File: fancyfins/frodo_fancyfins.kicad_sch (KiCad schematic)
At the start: 102 parts, among them J3 TC2050, U1 AZ1117-5.0, U10 L78L05_SOT89, U11 W25Q128JVP, U12 L78L05_SOT89, U13 L78L05_SOT89, U14 L78L05_SOT89, U15 L78L05_SOT89, U16 L78L05_SOT89, U2 AZ1117-3.3, U3 STM32F103RCTx, U4 MCP2562-E-SN, U5 TPD4E1U06, U6 L78L05_SOT89, U7 L78L05_SOT89, U8 L78L05_SOT89, U9 L78L05_SOT89, Y1 8MHz 12pF

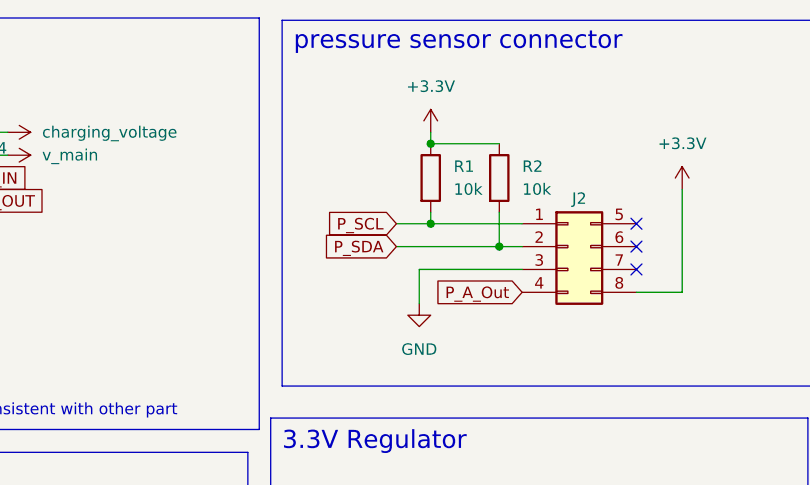
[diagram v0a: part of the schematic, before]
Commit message: finalized fancyfin routing (for now)
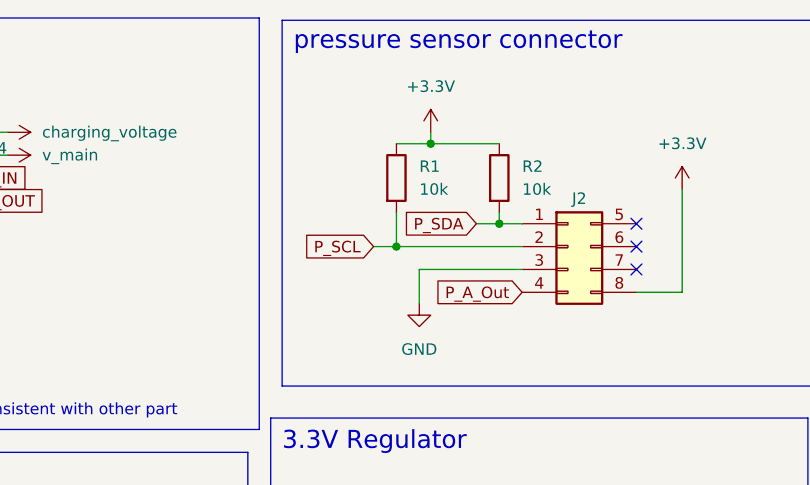
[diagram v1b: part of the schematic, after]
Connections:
- net P_SCL: now also J2.2 (Pin_2); no longer J2.1 (Pin_1)
- net P_SDA: now also J2.1 (Pin_1); no longer J2.2 (Pin_2)
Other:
- moved on the sheet: R1
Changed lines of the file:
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@@
 	)
 	(junction
+		(at 115.57 36.83)
+		(diameter 0)
+		(color 0 0 0 0)
+	)
+	(junction
 		(at 121.92 83.82)
 		(diameter 0)
@@
 	)
 	(junction
-		(at 107.95 36.83)
-		(diameter 0)
-		(color 0 0 0 0)
-	)
-	(junction
 		(at 46.99 214.63)
 		(diameter 0)
@@
 	)
 	(junction
-		(at 115.57 39.37)
-		(diameter 0)
-		(color 0 0 0 0)
-	)
-	(junction
 		(at 327.66 148.59)
 		(diameter 0)
@@
 	)
 	(junction
+		(at 104.14 39.37)
+		(diameter 0)
+		(color 0 0 0 0)
+	)
+	(junction
 		(at 109.22 231.14)
 		(diameter 0)
@@
 	(wire
 		(pts
-			(xy 107.95 35.56) (xy 107.95 36.83)
+			(xy 104.14 35.56) (xy 104.14 39.37)
 		)
 		(stroke
@@
 	(wire
 		(pts
-			(xy 104.14 39.37) (xy 115.57 39.37)
+			(xy 113.03 36.83) (xy 115.57 36.83)
 		)
 		(stroke
@@
 	(wire
 		(pts
-			(xy 115.57 35.56) (xy 115.57 39.37)
+			(xy 115.57 35.56) (xy 115.57 36.83)
 		)
 		(stroke
@@
 	(wire
 		(pts
+			(xy 115.57 36.83) (xy 118.11 36.83)
+		)
+		(stroke
+			(width 0)
+			(type default)
+		)
+	)
+	(wire
+		(pts
 			(xy 195.58 241.3) (xy 195.58 257.81)
 		)
@@
 	(wire
 		(pts
-			(xy 72.39 223.52) (xy 72.39 224.79)
+			(xy 104.14 27.94) (xy 107.95 27.94)
 		)
 		(stroke
@@
 	(wire
 		(pts
-			(xy 358.14 220.98) (xy 358.14 218.44)
+			(xy 72.39 223.52) (xy 72.39 224.79)
 		)
 		(stroke
@@
 	(wire
 		(pts
-			(xy 226.06 231.14) (xy 251.46 231.14)
+			(xy 358.14 220.98) (xy 358.14 218.44)
 		)
 		(stroke
@@
 	(wire
 		(pts
-			(xy 364.49 148.59) (xy 364.49 149.86)
+			(xy 226.06 231.14) (xy 251.46 231.14)
 		)
 		(stroke
@@
 	(wire
 		(pts
-			(xy 190.5 161.29) (xy 205.74 161.29)
+			(xy 364.49 148.59) (xy 364.49 149.86)
 		)
 		(stroke
@@
 	(wire
 		(pts
-			(xy 351.79 121.92) (xy 354.33 121.92)
+			(xy 190.5 161.29) (xy 205.74 161.29)
 		)
 		(stroke
@@
 	(wire
 		(pts
-			(xy 369.57 69.85) (xy 379.73 69.85)
+			(xy 351.79 121.92) (xy 354.33 121.92)
 		)
 		(stroke
@@
 	(wire
 		(pts
-			(xy 115.57 39.37) (xy 118.11 39.37)
+			(xy 369.57 69.85) (xy 379.73 69.85)
 		)
 		(stroke
@@
 	(wire
 		(pts
-			(xy 104.14 36.83) (xy 107.95 36.83)
+			(xy 101.6 39.37) (xy 104.14 39.37)
 		)
 		(stroke
@@
 	(wire
 		(pts
-			(xy 107.95 36.83) (xy 118.11 36.83)
-		)
-		(stroke
-			(width 0)
-			(type default)
-		)
-	)
-	(wire
-		(pts
 			(xy 142.24 224.79) (xy 142.24 223.52)
 		)
@@
 	(wire
 		(pts
+			(xy 104.14 39.37) (xy 118.11 39.37)
+		)
+		(stroke
+			(width 0)
+			(type default)
+		)
+	)
+	(wire
+		(pts
 			(xy 33.02 29.21) (xy 34.29 29.21)
 		)
@@
 	(global_label "P_SCL"
 		(shape input)
-		(at 104.14 36.83 180)
+		(at 101.6 39.37 180)
 		(fields_autoplaced yes)
 		(effects
@@
 		)
 		(property "Intersheetrefs" "${INTERSHEET_REFS}"
-			(at 95.4096 36.83 0)
+			(at 92.8696 39.37 0)
 			(effects
 				(font
@@
 	(global_label "P_SDA"
 		(shape input)
-		(at 104.14 39.37 180)
+		(at 113.03 36.83 180)
 		(fields_autoplaced yes)
 		(effects
@@
 		)
 		(property "Intersheetrefs" "${INTERSHEET_REFS}"
-			(at 95.3491 39.37 0)
+			(at 104.2391 36.83 0)
 			(effects
 				(font
@@
 	(symbol
 		(lib_id "Device:R")
-		(at 107.95 31.75 0)
+		(at 104.14 31.75 0)
 		(unit 1)
 		(exclude_from_sim no)
@@
 		(fields_autoplaced yes)
 		(property "Reference" "R1"
-			(at 110.49 30.4799 0)
+			(at 106.68 30.4799 0)
 			(effects
 				(font
@@
 		)
 		(property "Value" "10k"
-			(at 110.49 33.0199 0)
+			(at 106.68 33.0199 0)
 			(effects
 				(font
@@
 		)
 		(property "Footprint" "Resistor_SMD:R_0402_1005Metric"
-			(at 106.172 31.75 90)
+			(at 102.362 31.75 90)
 			(effects
 				(font
@@
 		)
 		(property "Datasheet" "~"
-			(at 107.95 31.75 0)
+			(at 104.14 31.75 0)
 			(effects
 				(font
@@
 		)
 		(property "Description" "Resistor"
-			(at 107.95 31.75 0)
+			(at 104.14 31.75 0)
 			(effects
 				(font

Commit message: finished routing for fin board
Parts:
- removed C17: 1u, Capacitor_SMD:C_0603_1608Metric_Pad1.08x0.95mm_HandSolder, symbol Device:C
- added C1: 330n, Capacitor_SMD:C_0402_1005Metric, symbol Device:C_Small
- added C2, C6, C7: 100n, Capacitor_SMD:C_0402_1005Metric, symbol Device:C_Small
- added C21: 1u, Capacitor_SMD:C_0402_1005Metric, symbol Device:C
- added JP1: SolderJumper_3_Open, Jumper:SolderJumper-3_P1.3mm_Open_RoundedPad1.0x1.5mm, symbol Jumper:SolderJumper_3_Open
- added R3: 10k, Resistor_SMD:R_0402_1005Metric, symbol Device:R
- added R9: 22, Resistor_SMD:R_0402_1005Metric, symbol Device:R_Small
- added U1: 78L05S, Package_TO_SOT_SMD:SOT-23, symbol Regulator_Linear:L78L05_SOT89
- added U3: TXB0102DCU, Package_SO:VSSOP-8_2.3x2mm_P0.5mm, symbol Logic_LevelTranslator:TXB0102DCU
- C19: renamed from C15; footprint Capacitor_SMD:C_0402_1005Metric_Pad0.74x0.62mm_HandSolder -> Capacitor_SMD:C_0402_1005Metric
- C20: renamed from C16; footprint Capacitor_SMD:C_0603_1608Metric_Pad1.08x0.95mm_HandSolder -> Capacitor_SMD:C_0402_1005Metric; LCSC# C15849 -> C14445
- D1: value SS34 -> SK34; LCSC # C466502 -> C5140034
- R4: renamed from R1; value 10k -> 4k7; footprint Resistor_SMD:R_0402_1005Metric -> Resistor_SMD:R_0603_1608Metric
- R5: renamed from R2; value 10k -> 4k7; footprint Resistor_SMD:R_0402_1005Metric -> Resistor_SMD:R_0603_1608Metric
- U2: renamed from U1; value AZ1117-5.0 -> AZ1117CH-3.3TRG1; LCSC# C526405 -> C92102
- renumbered C6 to C10, C7 to C11, C8 to C12, C9 to C13, C10 to C14, C11 to C15, C12 to C16, C13 to C17, C14 to C18, C18 to C22, C19 to C23, C20 to C24, C21 to C25, C23 to C26, C24 to C27, C25 to C28, C26 to C29, C1 to C3, C27 to C30, C22 to C31, C28 to C32, C29 to C33, C30 to C34, C31 to C35, C32 to C36, C33 to C37, C34 to C38, C35 to C39, C2 to C4, C36 to C40, C37 to C41, C38 to C42, C39 to C43, C40 to C44, C3 to C5, C4 to C8, C5 to C9, R3 to R1, R8 to R10, R9 to R11, R10 to R12, R11 to R13, R12 to R14, R4 to R2, R5 to R6, R6 to R7, R7 to R8, U8 to U10, U9 to U11, U10 to U12, U11 to U13, U12 to U14, U13 to U15, U14 to U16, U15 to U17, U16 to U18, U2 to U4, U3 to U5, U4 to U6, U5 to U7, U6 to U8, U7 to U9
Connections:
- net CAN_H_OUT is gone; now on net CAN_H_IN: J1.8 (Pin_8)
- net CAN_L_OUT is gone; now on net CAN_L_IN: J1.4 (Pin_4)
- net +3.3V: now also C12.2, U7.6 (V_{cc}), C21.1, C6.2, JP1.1 (A), U3.3 (VCCA); no longer J2.8 (Pin_8), U7.5 (IO4)
- net +5V: no longer C12.2, J3.10 (Pin_10), J3.9 (Pin_9), U7.6 (V_{cc})
- net CAN_RX: now also U5.44 (PA11); no longer U5.61 (PB8)
- net CAN_TX: now also U5.45 (PA12); no longer U5.62 (PB9)
- net GND: now also C1.1, C2.1, C21.2, C6.1, C7.1, R3.2, U1.3 (GND), U3.2 (GND)
- net J1-SWCLK: now also J3.6 (Pin_6), R11.1, U7.5 (IO4)
- net J1-SWDIO: now also U7.1 (IO1); no longer U7.2 (IO2)
- net J1-SWO: now also U7.4 (IO3); no longer U7.1 (IO1)
- net NRST: now also R9.1; no longer J3.1 (Pin_1)
- net P_A_Out: no longer J2.4 (Pin_4)
- net P_SCL: now also U5.58 (PB6), U3.5 (A1); no longer J2.2 (Pin_2), U5.29 (PB10)
- net P_SDA: now also U5.59 (PB7), U3.4 (A2); no longer J2.1 (Pin_1), U5.30 (PB11)
- net v_main: now also C1.2, U1.2 (IN)
- new net: J2.1 (Pin_1), U3.8 (B1)
- new net: J2.2 (Pin_2), U3.1 (B2)
- new net: C2.2, J2.8 (Pin_8), JP1.3 (B), U1.1 (OUT)
- new net: R3.1, U3.6 (OE)
- new net: C7.2, JP1.2 (C), U3.7 (VCCB)
- new net: J3.1 (Pin_1), R9.2, U7.2 (IO2)
- no-connect marks 41 -> 44
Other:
- note removed: "@TODO make sure that pin numbering is consistent with other part"
- moved on the sheet: C10, C4, C5, C9, D2, D3, J2, R1, R4, R5, R6, U2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

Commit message: some changes according to manu, added connector board
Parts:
- D4: value D_Schottky -> SK34; footprint Diode_SMD:D_SOD-123F -> Diode_SMD:D_SMA; LCSC# C167645 -> C5140034; Wert (none) -> SK34
- F1: value 1A -> 3A
- FB1: footprint Inductor_SMD:L_0603_1608Metric_Pad1.05x0.95mm_HandSolder -> Inductor_SMD:L_0402_1005Metric
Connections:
- net GND: now also J2.5 (Pin_5); no longer J2.3 (Pin_3)
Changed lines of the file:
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@@
 	)
 	(junction
-		(at 163.83 86.36)
-		(diameter 0)
-		(color 0 0 0 0)
-	)
-	(junction
 		(at 156.21 26.67)
 		(diameter 0)
@@
 	)
 	(junction
+		(at 185.42 81.28)
+		(diameter 0)
+		(color 0 0 0 0)
+	)
+	(junction
 		(at 223.52 39.37)
 		(diameter 0)
@@
 	)
 	(no_connect
-		(at 177.8 81.28)
-	)
-	(no_connect
 		(at 369.57 39.37)
 	)
@@
 	)
 	(no_connect
-		(at 177.8 83.82)
-	)
-	(no_connect
 		(at 369.57 100.33)
 	)
@@
 	)
 	(no_connect
+		(at 165.1 86.36)
+	)
+	(no_connect
+		(at 177.8 83.82)
+	)
+	(no_connect
 		(at 334.01 57.15)
 	)
@@
 	(wire
 		(pts
-			(xy 163.83 86.36) (xy 165.1 86.36)
-		)
-		(stroke
-			(width 0)
-			(type default)
-		)
-	)
-	(wire
-		(pts
 			(xy 379.73 64.77) (xy 369.57 64.77)
 		)
@@
 	(wire
 		(pts
-			(xy 162.56 86.36) (xy 163.83 86.36)
-		)
-		(stroke
-			(width 0)
-			(type default)
-		)
-	)
-	(wire
-		(pts
 			(xy 195.58 241.3) (xy 195.58 257.81)
 		)
@@
 	(wire
 		(pts
+			(xy 185.42 81.28) (xy 177.8 81.28)
+		)
+		(stroke
+			(width 0)
+			(type default)
+		)
+	)
+	(wire
+		(pts
 			(xy 38.1 198.12) (xy 38.1 199.39)
 		)
@@
 	(wire
 		(pts
-			(xy 163.83 86.36) (xy 163.83 90.17)
-		)
-		(stroke
-			(width 0)
-			(type default)
-		)
-	)
-	(wire
-		(pts
 			(xy 356.87 25.4) (xy 356.87 26.67)
 		)
@@
 	(wire
 		(pts
+			(xy 185.42 82.55) (xy 185.42 81.28)
+		)
+		(stroke
+			(width 0)
+			(type default)
+		)
+	)
+	(wire
+		(pts
 			(xy 394.97 148.59) (xy 394.97 147.32)
 		)
@@
 			)
 		)
-		(property "Footprint" "Inductor_SMD:L_0603_1608Metric_Pad1.05x0.95mm_HandSolder"
+		(property "Footprint" "Inductor_SMD:L_0402_1005Metric"
 			(at 384.81 140.208 90)
 			(effects
@@
 			)
 		)
-		(property "Value" "1A"
+		(property "Value" "3A"
 			(at 30.48 118.11 90)
 			(effects
@@
 	(symbol
 		(lib_id "power:PWR_FLAG")
-		(at 162.56 86.36 90)
+		(at 185.42 81.28 0)
 		(unit 1)
 		(exclude_from_sim no)
@@
 		(fields_autoplaced yes)
 		(property "Reference" "#FLG04"
-			(at 160.655 86.36 0)
+			(at 185.42 79.375 0)
 			(effects
 				(font
@@
 		)
 		(property "Value" "PWR_FLAG"
-			(at 158.75 86.3599 90)
+			(at 185.4201 77.47 90)
 			(effects
 				(font
@@
 		)
 		(property "Footprint" ""
-			(at 162.56 86.36 0)
+			(at 185.42 81.28 0)
 			(effects
 				(font
@@
 		)
 		(property "Datasheet" "~"
-			(at 162.56 86.36 0)
+			(at 185.42 81.28 0)
 			(effects
 				(font
@@
 		)
 		(property "Description" "Special symbol for telling ERC where power comes from"
-			(at 162.56 86.36 0)
+			(at 185.42 81.28 0)
 			(effects
 				(font
@@
 			)
 		)
-		(property "Value" "D_Schottky"
+		(property "Value" "SK34"
 			(at 41.91 118.11 0)
 			(effects
@@
 			)
 		)
-		(property "Footprint" "Diode_SMD:D_SOD-123F"
+		(property "Footprint" "Diode_SMD:D_SMA"
 			(at 41.91 120.65 0)
 			(effects
@@
 			)
 		)
-		(property "Datasheet" "~"
+		(property "Datasheet" "https://www.lcsc.com/datasheet/lcsc_datasheet_2410122031_MSKSEMI-SK34_C5140034.pdf"
 			(at 41.91 120.65 0)
 			(effects
@@
 			)
 		)
-		(property "Description" ""
+		(property "Description" "40V 3A Schottky Diode, SMA"
 			(at 41.91 120.65 0)
 			(effects
@@
 					(size 1.27 1.27)
 				)
+				(hide yes)
 			)
 		)
-		(property "Notes" ""
+		(property "Wert" "SK34"
 			(at 41.91 120.65 0)
 			(effects
@@
 			)
 		)
-		(property "LCSC#" "C167645"
+		(property "LCSC#" "C5140034"
 			(at 41.91 120.65 0)
 			(effects
@@
 		(lib_name "GND_1")
 		(lib_id "power:GND")
-		(at 163.83 90.17 0)
+		(at 185.42 82.55 0)
 		(unit 1)
 		(exclude_from_sim no)
@@
 		(on_board yes)
 		(dnp no)
-		(fields_autoplaced yes)
 		(property "Reference" "#PWR033"
-			(at 163.83 96.52 0)
+			(at 185.42 88.9 0)
 			(effects
 				(font
@@
 		)
 		(property "Value" "GND"
-			(at 163.83 95.25 0)
+			(at 185.42 86.106 0)
 			(effects
 				(font
@@
 		)
 		(property "Footprint" ""
-			(at 163.83 90.17 0)
+			(at 185.42 82.55 0)
 			(effects
 				(font
@@
 		)
 		(property "Datasheet" ""
-			(at 163.83 90.17 0)
+			(at 185.42 82.55 0)
 			(effects
 				(font
@@
 		)
 		(property "Description" "Power symbol creates a global label with name \"GND\" , ground"
-			(at 163.83 90.17 0)
+			(at 185.42 82.55 0)
 			(effects
 				(font
@@
 		)
 		(instances
-			(project ""
+			(project "frodo_fancyfins"
 				(path "/6b822b14-450b-45c3-a34b-8e18c5811754"
 					(reference "#PWR033")
